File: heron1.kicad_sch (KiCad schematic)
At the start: 16 parts, among them J3 MotorA, J4 Motor B, J5 VNH5019, J9 VNH5019, SW1 SW_Push, U1 DRV8835

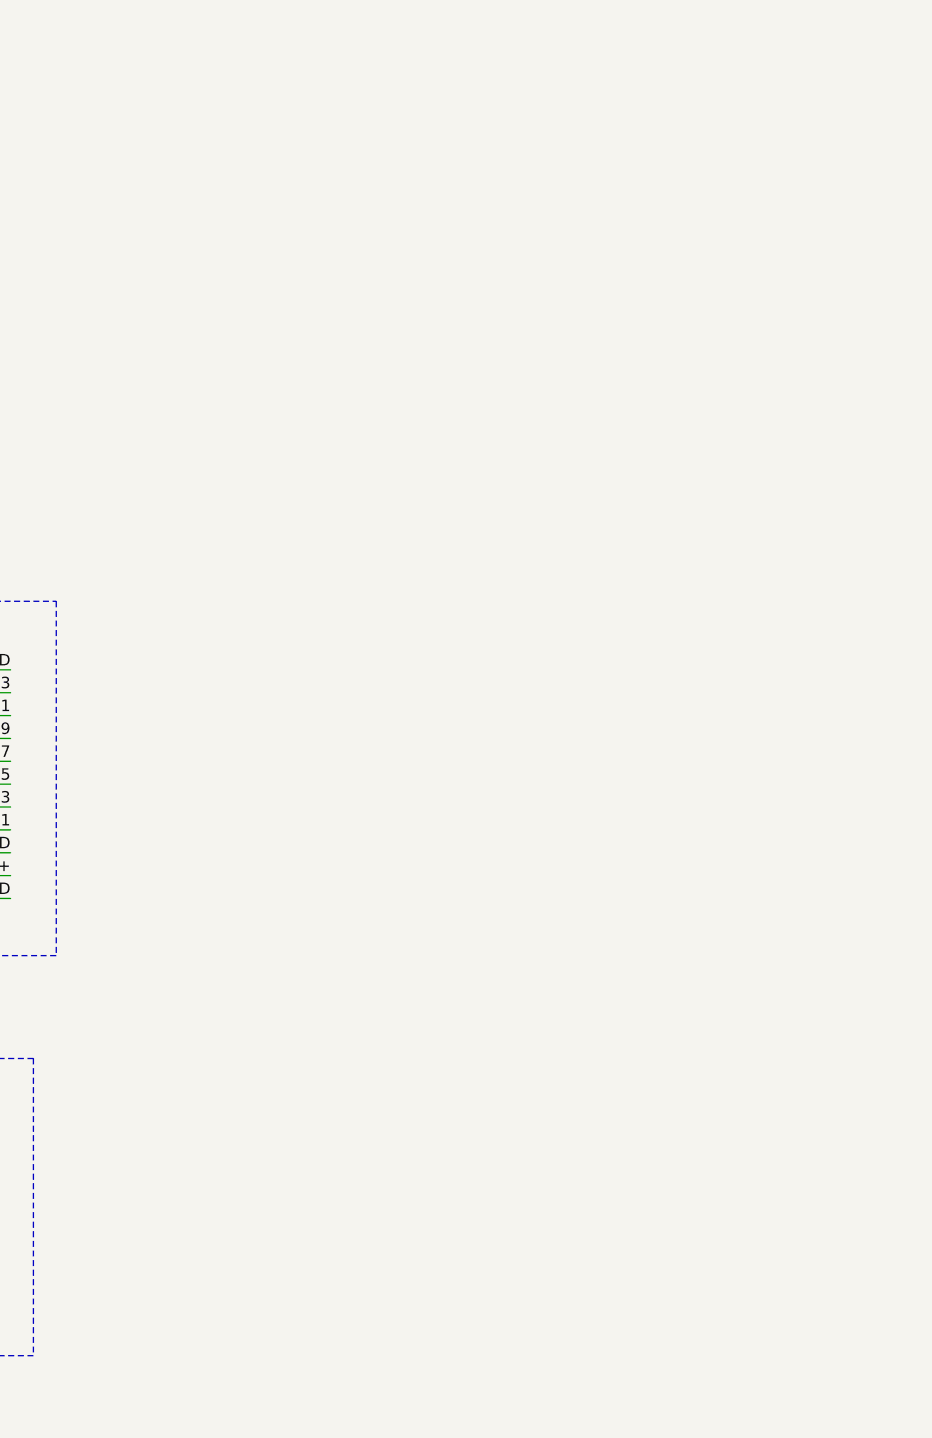
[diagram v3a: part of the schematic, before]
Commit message: custom drivers created
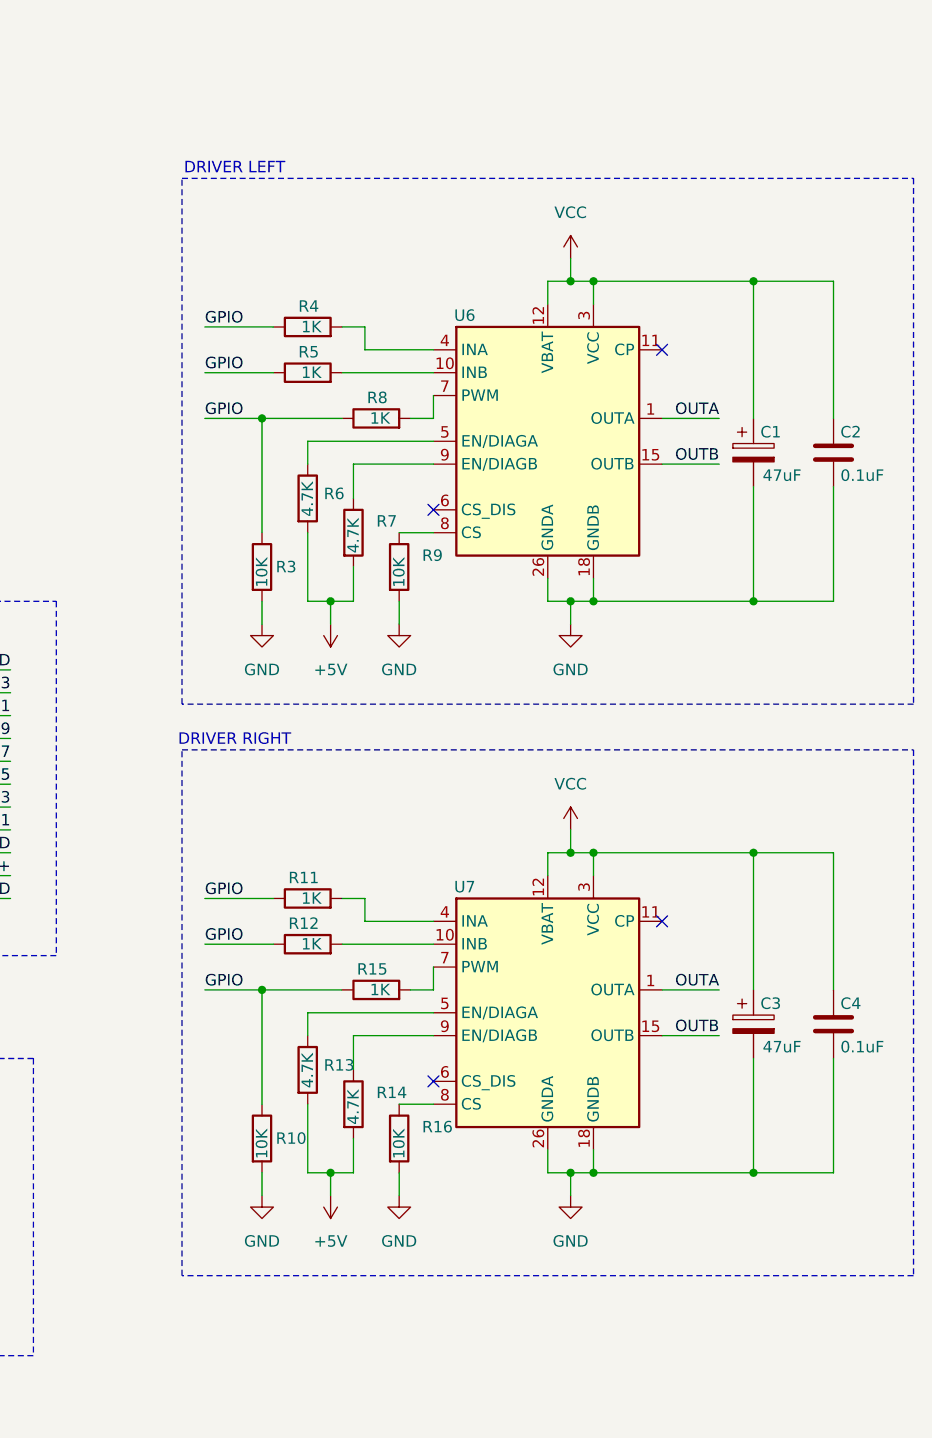
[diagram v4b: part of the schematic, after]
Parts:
- added C1, C3: 47uF, symbol Device:C_Polarized
- added C2, C4: 0.1uF, symbol Device:C
- added R10, R16, R3, R9: 10K, symbol Device:R
- added R11, R12, R15, R4, R5, R8: 1K, symbol Device:R
- added R13, R14, R6, R7: 4.7K, symbol Device:R
- added U6, U7: VNH5019A-E, Package_SO:ST_MultiPowerSO-30, symbol Driver_Motor:VNH5019A-E
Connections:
- net GND: now also C1.2, C2.2, C3.2, C4.2, R10.2, R16.2, R3.2, R9.2, U6.18 (GNDB), U6.19 (GNDB), U6.20 (GNDB), U6.26 (GNDA), U6.27 (GNDA), U6.28 (GNDA), U7.18 (GNDB), U7.19 (GNDB), U7.20 (GNDB), U7.26 (GNDA), U7.27 (GNDA), U7.28 (GNDA)
- new net: R8.2, U6.7 (PWM)
- new net: R15.2, U7.7 (PWM)
- new net: R6.1, U6.5 (EN/DIAGA)
- new net: R5.2, U6.10 (INB)
- new net: R12.2, U7.10 (INB)
- new net: R7.1, U6.9 (EN/DIAGB)
- new net: R4.2, U6.4 (INA)
- new net: R13.1, U7.5 (EN/DIAGA)
- new net: R11.2, U7.4 (INA)
- new net: R16.1, U7.8 (CS)
- new net: R14.1, U7.9 (EN/DIAGB)
- new net: R9.1, U6.8 (CS)
- new net +5V: R13.2, R14.2, R6.2, R7.2
- new net GPIO: R10.1, R11.1, R12.1, R15.1, R3.1, R4.1, R5.1, R8.1
- new net OUTA: U6.1 (OUTA), U6.25 (OUTA), U6.30 (OUTA), U6.33 (OUTA), U7.1 (OUTA), U7.25 (OUTA), U7.30 (OUTA), U7.33 (OUTA)
- new net OUTB: U6.15 (OUTB), U6.16 (OUTB), U6.21 (OUTB), U6.32 (OUTB), U7.15 (OUTB), U7.16 (OUTB), U7.21 (OUTB), U7.32 (OUTB)
- new net VCC: C1.1, C2.1, C3.1, C4.1, U6.12 (VBAT), U6.13 (VCC), U6.23 (VCC), U6.3 (VCC), U6.31 (VCC), U7.12 (VBAT), U7.13 (VCC), U7.23 (VCC), U7.3 (VCC), U7.31 (VCC)
- no-connect marks 7 -> 11
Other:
- note added: "DRIVER LEFT"
- note added: "DRIVER RIGHT"

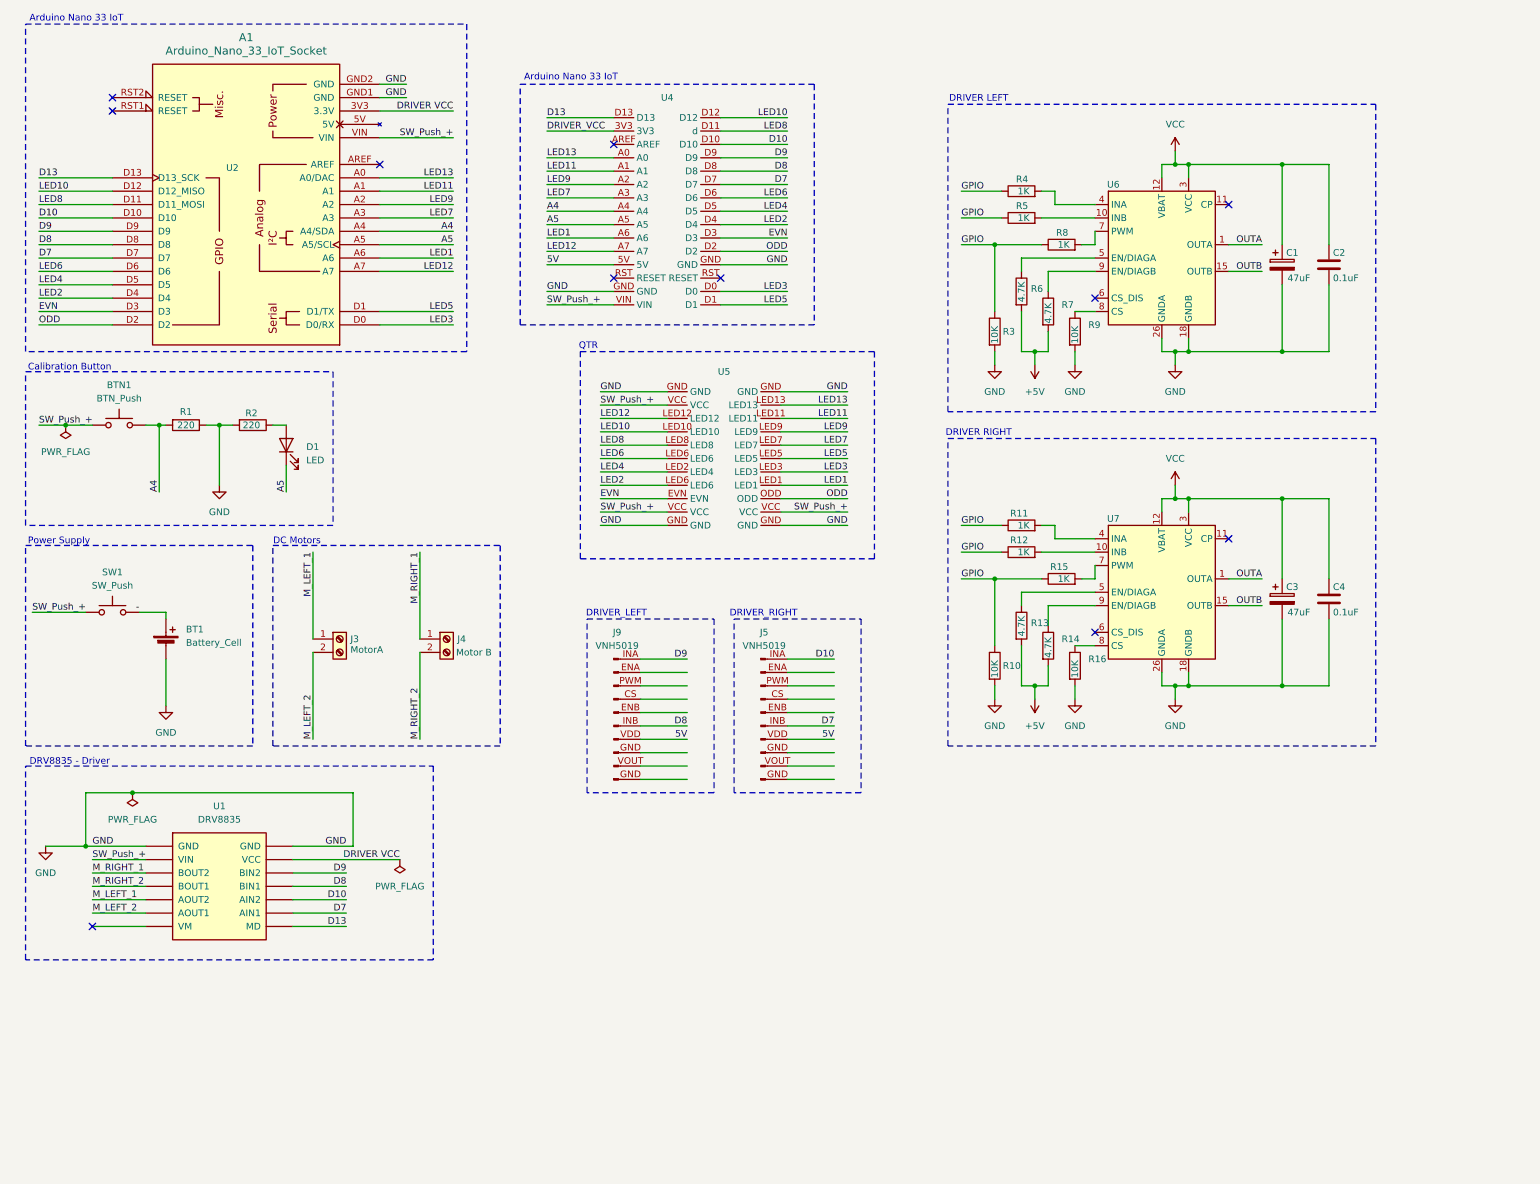
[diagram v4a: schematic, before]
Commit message: Updated version of pcb to use esp32 s3 devkitc-1
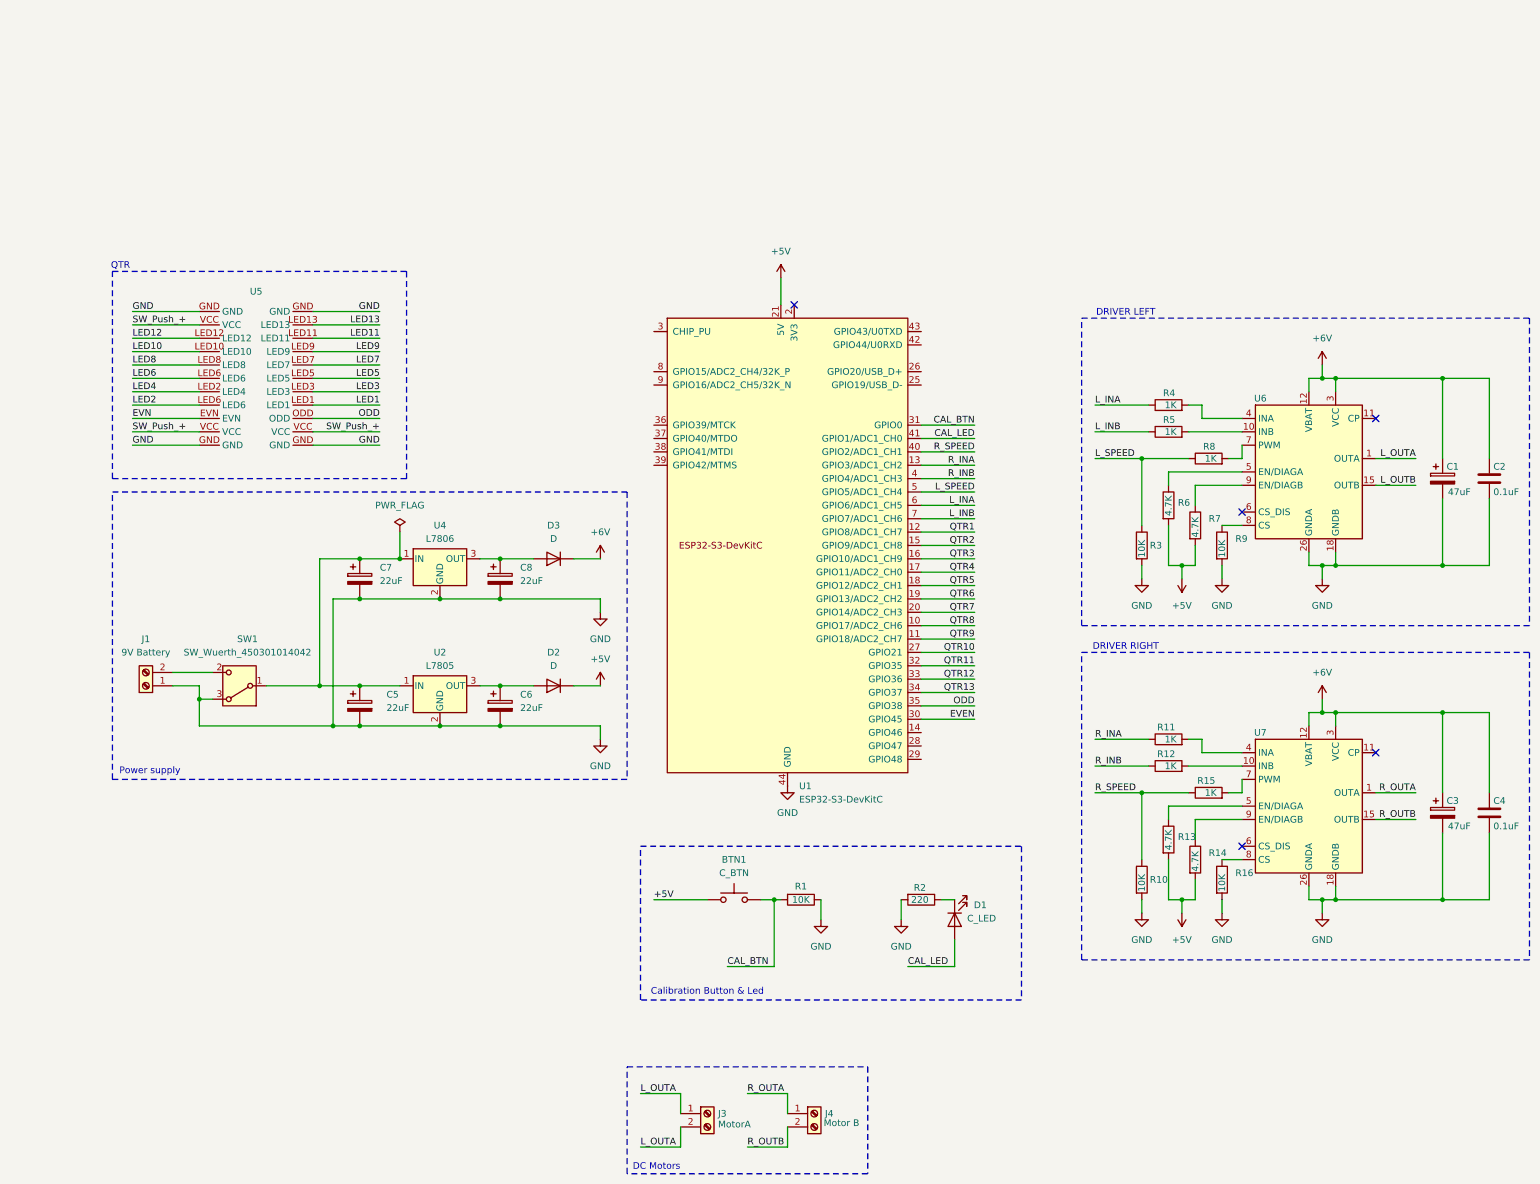
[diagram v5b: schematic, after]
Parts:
- removed A1: Arduino_Nano_33_IoT_Socket, PCM_arduino-library:Arduino_Nano_33_IoT_Socket, symbol PCM_arduino-library:Arduino_Nano_33_IoT_Socket
- removed BT1: Battery_Cell, Connector_JST:JST_PH_B2B-PH-K_1x02_P2.00mm_Vertical, symbol Device:Battery_Cell
- removed J5, J9: VNH5019, symbol heron_symbols:VNH5019
- removed SW1: SW_Push, symbol Switch:SW_Push
- removed U1: DRV8835, symbol Driver_Motor:DRV8833RTY
- removed U2: ~, symbol heron_symbols:Arduino_Nano_33_Iot
- removed U3, U4: ~, symbol heron_symbols:Arduino_Nano_33_IoT
- added C5, C6, C7, C8: 22uF, Capacitor_SMD:CP_Elec_4x3, symbol Device:C_Polarized
- added D2, D3: D, Diode_SMD:D_1206_3216Metric, symbol Device:D
- added J1: 9V Battery, TerminalBlock_Phoenix:TerminalBlock_Phoenix_MPT-0,5-2-2.54_1x02_P2.54mm_Horizontal, symbol Connector:Screw_Terminal_01x02
- added SW1: SW_Wuerth_450301014042, Button_Switch_THT:SW_Slide-03_Wuerth-WS-SLTV_10x2.5x6.4_P2.54mm, symbol Switch:SW_Wuerth_450301014042
- added U1: ESP32-S3-DevKitC, PCM_Espressif:ESP32-S3-DevKitC, symbol PCM_Espressif:ESP32-S3-DevKitC
- added U2: L7805, Package_TO_SOT_SMD:TO-252-2, symbol Regulator_Linear:L7805
- added U4: L7806, symbol Regulator_Linear:L7806
- BTN1: value BTN_Push -> C_BTN
- D1: value LED -> C_LED
- R1: value 220 -> 10K
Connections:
- net A5 is gone; now on an unnamed net: D1.1 (K)
- net M_LEFT_2 is gone; now on net L_OUTA: J3.2 (Pin_2)
- net +5V: now also BTN1.1, D2.1 (K), U1.21 (5V)
- net GND: now also C5.2, C6.2, C7.2, C8.2, J1.1 (Pin_1), SW1.3 (A), U1.22 (GND), U1.23 (GND), U1.24 (GND), U1.44 (GND), U2.2 (GND), U4.2 (GND)
- net ODD: now also U1.35 (GPIO38)
- net SW_Push_+: no longer BTN1.1
- net at R2.1: no longer D1.2 (A)
- net A4 renamed CAL_BTN
- net CAL_BTN: now also U1.31 (GPIO0)
- removed net GPIO: R10.1, R11.1, R12.1, R15.1, R3.1, R4.1, R5.1, R8.1
- net M_LEFT_1 renamed L_OUTA
- net L_OUTA: now also U6.1 (OUTA), U6.25 (OUTA), U6.30 (OUTA), U6.33 (OUTA)
- net M_RIGHT_1 renamed R_OUTA
- net R_OUTA: now also U7.1 (OUTA), U7.25 (OUTA), U7.30 (OUTA), U7.33 (OUTA)
- net M_RIGHT_2 renamed R_OUTB
- net R_OUTB: now also U7.15 (OUTB), U7.16 (OUTB), U7.21 (OUTB), U7.32 (OUTB)
- removed net OUTA: U6.1 (OUTA), U6.25 (OUTA), U6.30 (OUTA), U6.33 (OUTA), U7.1 (OUTA), U7.25 (OUTA), U7.30 (OUTA), U7.33 (OUTA)
- net OUTB renamed L_OUTB
- net L_OUTB: no longer U7.15 (OUTB), U7.16 (OUTB), U7.21 (OUTB), U7.32 (OUTB)
- net VCC renamed +6V
- net +6V: now also D3.1 (K)
- new net: C8.1, D3.2 (A), U4.3 (OUT)
- new net: J1.2 (Pin_2), SW1.2 (C)
- new net: C5.1, C7.1, SW1.1 (B), U2.1 (IN), U4.1 (IN)
- new net: U1.1 (3V3), U1.2 (3V3)
- new net: C6.1, D2.2 (A), U2.3 (OUT)
- new net CAL_LED: D1.2 (A), U1.41 (GPIO1/ADC1_CH0)
- new net EVEN: U1.30 (GPIO45)
- new net L_INA: R4.1, U1.6 (GPIO6/ADC1_CH5)
- new net L_INB: R5.1, U1.7 (GPIO7/ADC1_CH6)
- new net L_SPEED: R3.1, R8.1, U1.5 (GPIO5/ADC1_CH4)
- new net QTR1: U1.12 (GPIO8/ADC1_CH7)
- new net QTR10: U1.27 (GPIO21)
- new net QTR11: U1.32 (GPIO35)
- new net QTR12: U1.33 (GPIO36)
- new net QTR13: U1.34 (GPIO37)
- new net QTR2: U1.15 (GPIO9/ADC1_CH8)
- new net QTR3: U1.16 (GPIO10/ADC1_CH9)
- new net QTR4: U1.17 (GPIO11/ADC2_CH0)
- new net QTR5: U1.18 (GPIO12/ADC2_CH1)
- new net QTR6: U1.19 (GPIO13/ADC2_CH2)
- new net QTR7: U1.20 (GPIO14/ADC2_CH3)
- new net QTR8: U1.10 (GPIO17/ADC2_CH6)
- new net QTR9: U1.11 (GPIO18/ADC2_CH7)
- new net R_INA: R11.1, U1.13 (GPIO3/ADC1_CH2)
- new net R_INB: R12.1, U1.4 (GPIO4/ADC1_CH3)
- new net R_SPEED: R10.1, R15.1, U1.40 (GPIO2/ADC1_CH1)
- no-connect marks 11 -> 5
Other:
- note added: "Calibration Button & Led"
- note added: "Power supply"
- note removed: "Arduino Nano 33 IoT"
- note removed: "Calibration Button"
- note removed: "DRIVER_LEFT"
- note removed: "DRIVER_RIGHT"
- note removed: "DRV8835 - Driver"
- note removed: "Power Supply"
- moved on the sheet: BTN1, C1, C2, C3, C4, D1, J3, J4, R1, R10, R11, R12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

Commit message: Updated PCB layout
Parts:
- removed U5: ~, symbol heron_symbols:QTR_13
- added J2: Conn_02x11_Counter_Clockwise, Connector_FFC-FPC:TE_2-84952-2_1x22-1MP_P1.0mm_Horizontal, symbol Connector_Generic:Conn_02x11_Counter_Clockwise
- C1, C3: footprint (none) -> Capacitor_THT:CP_Radial_D5.0mm_P2.50mm
- C2, C4: footprint (none) -> Capacitor_SMD:C_0603_1608Metric
- C5, C6, C7, C8: footprint Capacitor_SMD:CP_Elec_4x3 -> Capacitor_THT:CP_Radial_D5.0mm_P2.50mm
- D1: footprint LED_THT:LED_D5.0mm_Clear -> LED_SMD:LED_0805_2012Metric
- J1: value 9V Battery -> 7.4 V BAT
- J3, J4: footprint (none) -> TerminalBlock_Phoenix:TerminalBlock_Phoenix_MPT-0,5-2-2.54_1x02_P2.54mm_Horizontal
- R1, R10, R16, R3, R9: footprint (none) -> Resistor_SMD:R_1206_3216Metric
- R11, R12, R15, R4, R5, R8: footprint (none) -> Resistor_SMD:R_0402_1005Metric
- R13, R14, R6, R7: footprint (none) -> Resistor_SMD:R_0805_2012Metric
- R2: footprint (none) -> Resistor_SMD:R_0603_1608Metric
- U4: footprint (none) -> Package_TO_SOT_SMD:TO-252-2
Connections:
- net +5V: now also J2.10 (Pin_10), J2.13 (Pin_13), J2.2 (Pin_2)
- net EVEN: now also J2.9 (Pin_9)
- net GND: now also J2.1 (Pin_1), J2.11 (Pin_11), J2.12 (Pin_12), J2.22 (Pin_22)
- net ODD: now also J2.14 (Pin_14)
- net QTR1: now also J2.15 (Pin_15)
- net QTR10: now also J2.4 (Pin_4)
- net QTR11: now also J2.20 (Pin_20)
- net QTR12: now also J2.3 (Pin_3)
- net QTR13: now also J2.21 (Pin_21)
- net QTR2: now also J2.8 (Pin_8)
- net QTR3: now also J2.16 (Pin_16)
- net QTR4: now also J2.7 (Pin_7)
- net QTR5: now also J2.17 (Pin_17)
- net QTR6: now also J2.6 (Pin_6)
- net QTR7: now also J2.18 (Pin_18)
- net QTR8: now also J2.5 (Pin_5)
- net QTR9: now also J2.19 (Pin_19)
- no-connect marks 5 -> 19
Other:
- moved on the sheet: J3, J4

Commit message: first stage pcb
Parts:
- added C9: C, Capacitor_SMD:C_0805_2012Metric, symbol Device:C
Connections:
- net +5V: now also C9.1
- net GND: now also C9.2
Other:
- moved on the sheet: U1
